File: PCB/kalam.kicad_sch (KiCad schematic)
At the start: 17 parts, among them J1 Conn_01x04, J2 Conn_01x04, SW1 SW_Push, SW2 SW_Push, U1 XC6206PxxxMR, U2 STM32F072CBTx

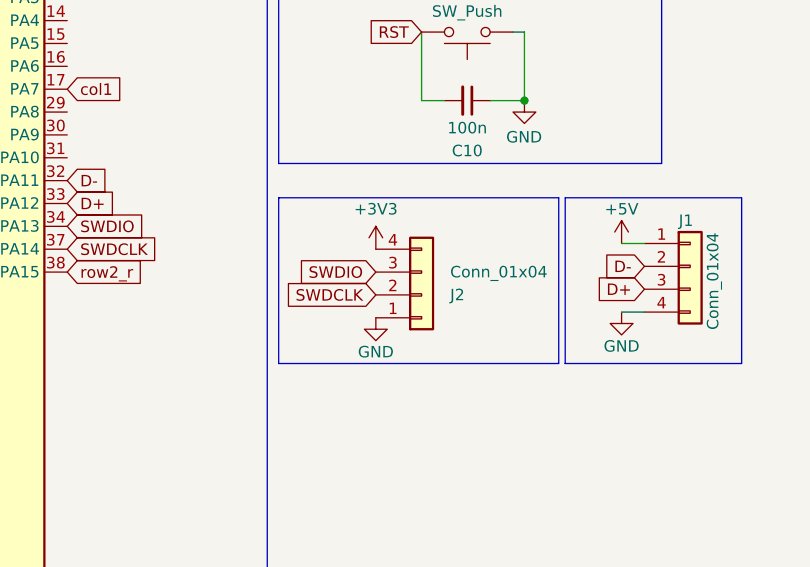
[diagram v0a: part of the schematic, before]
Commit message: More files added
Gerber files for PCB along with BOM and CPL files. Also added picture of supported layouts
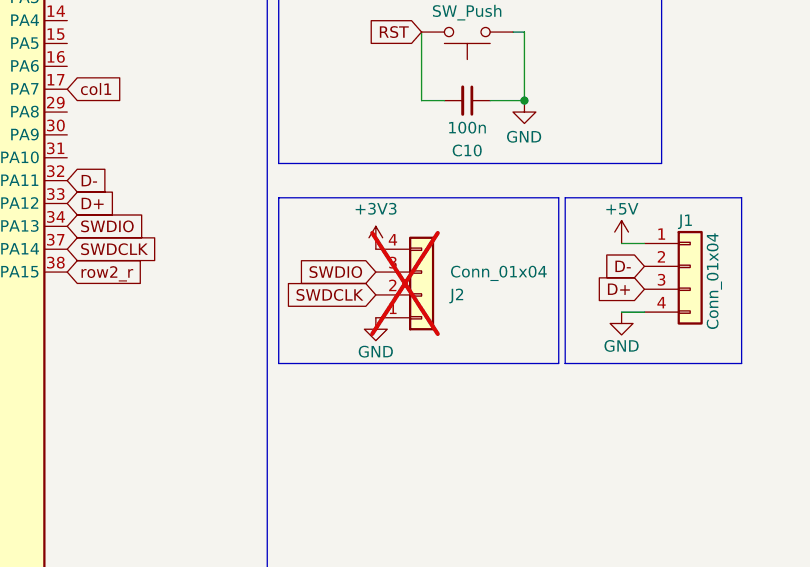
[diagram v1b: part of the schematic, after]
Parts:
- J2: now not fitted
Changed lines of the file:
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@@
 		(in_bom yes)
 		(on_board yes)
-		(dnp no)
+		(dnp yes)
 		(property "Reference" "J2"
 			(at 108.585 95.25 0)
@@
 		)
 		(instances
-			(project "arkre"
+			(project "kalam"
 				(path "/3657237e-c8f2-4ecf-b631-303d8d00a2b6"
 					(page "2")

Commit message: PCB Fab v1
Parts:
- C1, C10, C2, C4: LCSC C1525 -> (none)
- C3, C5: LCSC C19666 -> (none)
- C6: LCSC C15195 -> (none)
- C7, C8, C9: LCSC C52923 -> (none)
- J1: LCSC C160404 -> (none)
- J2: now fitted
- R1: LCSC C25744 -> (none)
- SW1, SW2: LCSC C318884 -> (none)
- U1: LCSC C5148692 -> (none)
- U2: LCSC C81720 -> (none)
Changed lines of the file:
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@@
-			)
-		)
-		(property "LCSC" "C318884"
-			(at 110.49 24.13 0)
-			(effects
-				(font
-					(size 1.27 1.27)
-				)
-				(hide yes)
 			)
 		)
@@
 			)
 		)
-		(property "LCSC" "C318884"
-			(at 110.49 66.04 0)
-			(effects
-				(font
-					(size 1.27 1.27)
-				)
-				(hide yes)
-			)
-		)
 		(pin "1"
 		)
@@
 		)
 		(property "Description" ""
-			(at 135.255 92.075 0)
-			(effects
-				(font
-					(size 1.27 1.27)
-				)
-				(hide yes)
-			)
-		)
-		(property "LCSC" "C160404"
 			(at 135.255 92.075 0)
 			(effects
@@
 			)
 		)
-		(property "LCSC" "C25744"
-			(at 118.11 26.67 0)
-			(effects
-				(font
-					(size 1.27 1.27)
-				)
-				(hide yes)
-			)
-		)
 		(pin "1"
 		)
@@
 			)
 		)
-		(property "LCSC" "C19666"
-			(at 45.085 24.13 0)
-			(effects
-				(font
-					(size 1.27 1.27)
-				)
-				(hide yes)
-			)
-		)
 		(pin "1"
 		)
@@
 			)
 		)
-		(property "LCSC" "C1525"
-			(at 36.83 24.13 0)
-			(effects
-				(font
-					(size 1.27 1.27)
-				)
-				(hide yes)
-			)
-		)
 		(pin "1"
 		)
@@
 			)
 		)
-		(property "LCSC" "C1525"
-			(at 28.575 24.13 0)
-			(effects
-				(font
-					(size 1.27 1.27)
-				)
-				(hide yes)
-			)
-		)
 		(pin "1"
 		)
@@
 			)
 		)
-		(property "LCSC" "C1525"
-			(at 36.83 35.56 0)
-			(effects
-				(font
-					(size 1.27 1.27)
-				)
-				(hide yes)
-			)
-		)
 		(pin "1"
 		)
@@
 		)
 		(property "Description" ""
-			(at 123.19 46.99 0)
-			(effects
-				(font
-					(size 1.27 1.27)
-				)
-				(hide yes)
-			)
-		)
-		(property "LCSC" "C52923"
 			(at 123.19 46.99 0)
 			(effects
@@
 			)
 		)
-		(property "LCSC" "C52923"
-			(at 66.675 37.465 0)
-			(effects
-				(font
-					(size 1.27 1.27)
-				)
-				(hide yes)
-			)
-		)
 		(pin "1"
 		)
@@
 			)
 		)
-		(property "LCSC" "C5148692"
-			(at 110.49 44.45 0)
-			(effects
-				(font
-					(size 1.27 1.27)
-				)
-				(hide yes)
-			)
-		)
 		(pin "1"
 		)
@@
 		)
 		(property "Description" ""
-			(at 58.42 37.465 0)
-			(effects
-				(font
-					(size 1.27 1.27)
-				)
-				(hide yes)
-			)
-		)
-		(property "LCSC" "C15195"
 			(at 58.42 37.465 0)
 			(effects
@@
 			)
 		)
-		(property "LCSC" "C1525"
-			(at 110.49 73.66 0)
-			(effects
-				(font
-					(size 1.27 1.27)
-				)
-				(hide yes)
-			)
-		)
 		(pin "1"
 		)
@@
 		(in_bom yes)
 		(on_board yes)
-		(dnp yes)
+		(dnp no)
 		(property "Reference" "J2"
 			(at 108.585 95.25 0)
@@
 			)
 		)
-		(property "LCSC" "C81720"
-			(at 48.26 90.17 0)
-			(effects
-				(font
-					(size 1.27 1.27)
-				)
-				(hide yes)
-			)
-		)
 		(pin "23"
 		)
@@
 			)
 		)
-		(property "LCSC" "C52923"
-			(at 97.79 46.99 0)
-			(effects
-				(font
-					(size 1.27 1.27)
-				)
-				(hide yes)
-			)
-		)
 		(pin "1"
 		)
@@
 			(at 45.085 35.56 0)
 			(effects
-				(font
-					(size 1.27 1.27)
-				)
-				(hide yes)
-			)
-		)
-		(property "LCSC" "C19666"
-			(at 45.085 35.56 0)
-			(effects

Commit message: updates
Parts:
- removed SW2: SW_Push, Button_Switch_SMD:SW_Push_1P1T_XKB_TS-1187A, symbol Switch:SW_Push
- C5: value 4.7u -> 1u
- C7: value 1u -> 4.7u
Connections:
- net col12 is gone; now on net col3: U2.46 (PB9)
- net col11: now also U2.43 (PB7); no longer U2.45 (PB8)
- net col3: no longer U2.39 (PB3)
- net col4: now also U2.45 (PB8); no longer U2.2 (PC13)
- net col6: now also U2.39 (PB3); no longer U2.40 (PB4)
- net col7: now also U2.40 (PB4); no longer U2.41 (PB5)
- net col8: now also U2.41 (PB5); no longer U2.42 (PB6)
- net col9: now also U2.42 (PB6); no longer U2.43 (PB7)
- net RST: no longer names the net of C10.2, U2.7 (NRST)

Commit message: back to the drawing board
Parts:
- removed J2: Conn_01x04, Connector_PinHeader_2.54mm:PinHeader_1x04_P2.54mm_Vertical, symbol Connector_Generic:Conn_01x04
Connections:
- net SWDCLK is gone; now on net col10: U2.37 (PA14)
- net SWDIO is gone; now on net row0: U2.34 (PA13)
- net col0: no longer U2.19 (PB1)
- net col1: no longer U2.17 (PA7)
- net col10: no longer U2.27 (PB14)
- net col11: no longer U2.43 (PB7)
- net col2: no longer U2.3 (PC14)
- net col3: no longer U2.46 (PB9)
- net col4: no longer U2.45 (PB8)
- net col5: no longer U2.26 (PB13)
- net col6: no longer U2.39 (PB3)
- net col7: no longer U2.40 (PB4)
- net col8: no longer U2.41 (PB5)
- net col9: now also U2.4 (PC15); no longer U2.42 (PB6)
- net row0: no longer U2.25 (PB12)
- net row1: now also U2.25 (PB12); no longer U2.20 (PB2)
- net row3: no longer U2.4 (PC15)
- net row2_l: no longer names the net of U2.18 (PB0)
- net row2_r: no longer names the net of U2.38 (PA15)
- new net row2: U2.3 (PC14)
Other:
- moved on the sheet: C1, C10, C2, C4, C5, C6, C7, C8, C9, J1, R1, SW1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

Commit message: beeg overhaul and new layout image
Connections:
- net col0: now also U2.21 (PB10)
- net col1: now also U2.19 (PB1)
- net col11: now also U2.38 (PA15)
- net col2: now also U2.17 (PA7)
- net col3: now also U2.43 (PB7)
- net col4: now also U2.42 (PB6)
- net col5: now also U2.15 (PA5)
- net col6: now also U2.41 (PB5)
- net col7: now also U2.40 (PB4)
- net col8: now also U2.13 (PA3)
- net row3: now also U2.39 (PB3)
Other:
- moved on the sheet: C6, C7
